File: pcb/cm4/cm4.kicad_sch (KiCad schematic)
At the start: 1 part, among them J101 Conn_02x10_Row_Letter_First

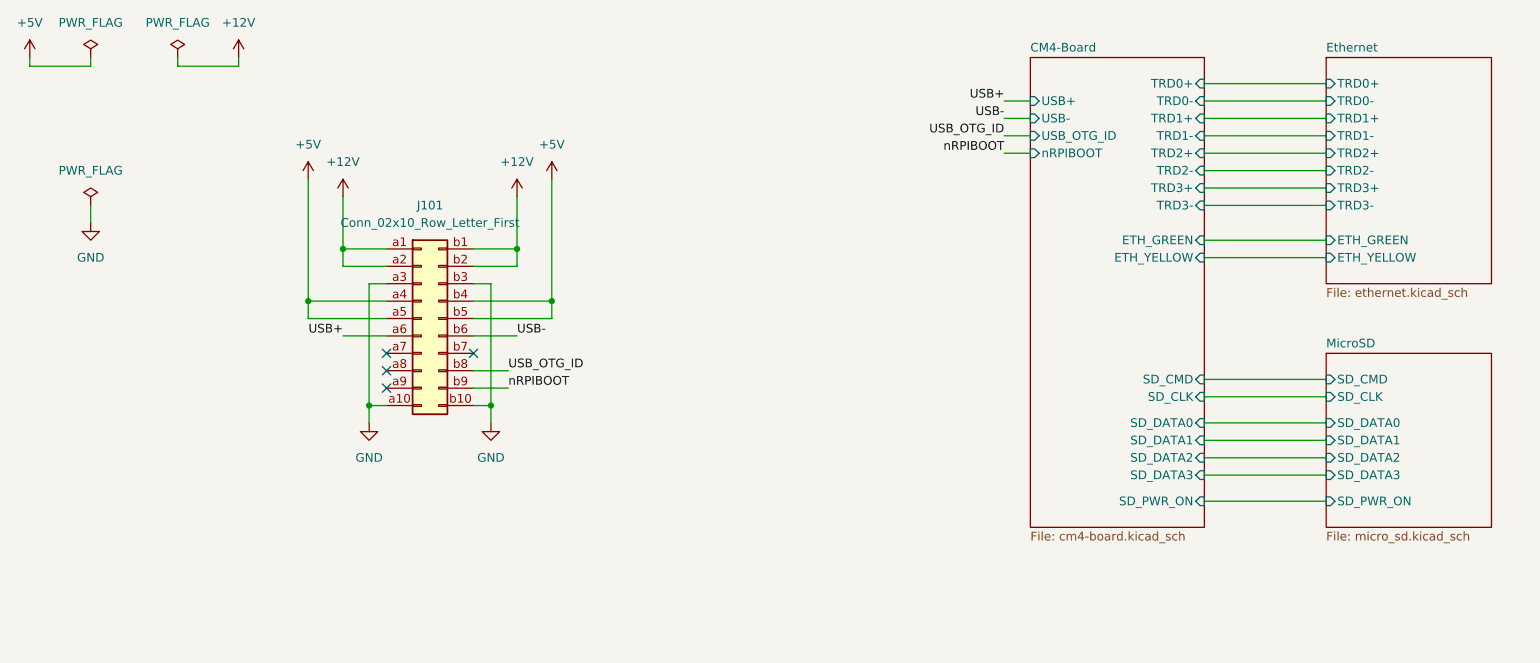
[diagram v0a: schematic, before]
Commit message: add i2c
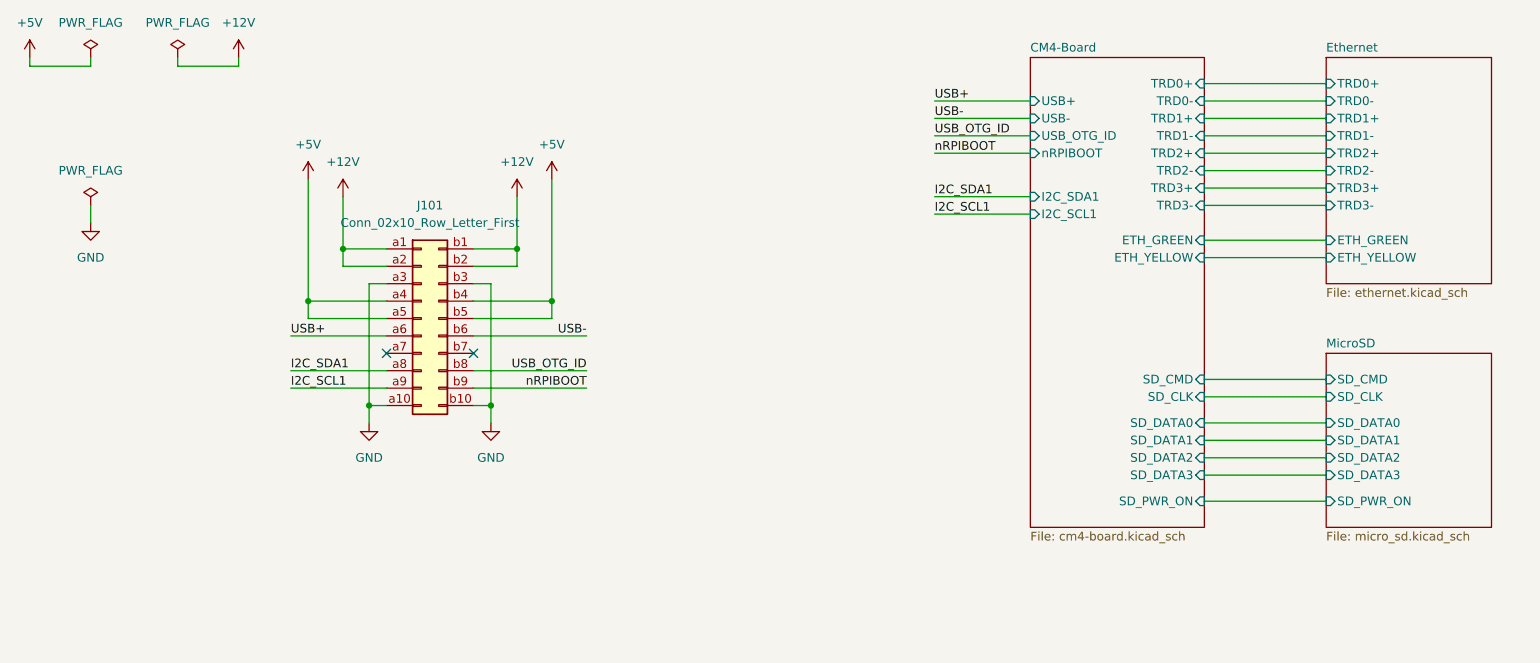
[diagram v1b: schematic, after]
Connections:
- net I2C_SDA1: now reaches J101.a8 (Pin_a8)
- net I2C_SCL1: now reaches J101.a9 (Pin_a9)
- no-connect marks 4 -> 2
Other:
- sheet CM4-Board ports: added I2C_SCL1, I2C_SDA1; removed none
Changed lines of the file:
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@@
-	)
-	(no_connect
-		(at 76.2 115.57)
 	)
 	(no_connect
 		(at 76.2 113.03)
 	)
-	(no_connect
-		(at 76.2 118.11)
-	)
 	(wire
 		(pts
@@
 	(wire
 		(pts
-			(xy 166.37 78.74) (xy 170.18 78.74)
+			(xy 156.21 78.74) (xy 170.18 78.74)
 		)
 		(stroke
@@
 	(wire
 		(pts
-			(xy 69.85 110.49) (xy 76.2 110.49)
+			(xy 62.23 110.49) (xy 76.2 110.49)
 		)
 		(stroke
@@
 	(wire
 		(pts
-			(xy 166.37 83.82) (xy 170.18 83.82)
+			(xy 156.21 83.82) (xy 170.18 83.82)
 		)
 		(stroke
@@
 	(wire
 		(pts
-			(xy 166.37 76.2) (xy 170.18 76.2)
+			(xy 156.21 76.2) (xy 170.18 76.2)
 		)
 		(stroke
@@
 	(wire
 		(pts
-			(xy 88.9 118.11) (xy 93.98 118.11)
+			(xy 156.21 92.71) (xy 170.18 92.71)
+		)
+		(stroke
+			(width 0)
+			(type default)
+		)
+	)
+	(wire
+		(pts
+			(xy 156.21 90.17) (xy 170.18 90.17)
+		)
+		(stroke
+			(width 0)
+			(type default)
+		)
+	)
+	(wire
+		(pts
+			(xy 88.9 118.11) (xy 105.41 118.11)
 		)
 		(stroke
@@
 	(wire
 		(pts
+			(xy 62.23 118.11) (xy 76.2 118.11)
+		)
+		(stroke
+			(width 0)
+			(type default)
+		)
+	)
+	(wire
+		(pts
 			(xy 95.25 97.79) (xy 95.25 90.17)
 		)
@@
 	(wire
 		(pts
+			(xy 62.23 115.57) (xy 76.2 115.57)
+		)
+		(stroke
+			(width 0)
+			(type default)
+		)
+	)
+	(wire
+		(pts
 			(xy 95.25 100.33) (xy 95.25 97.79)
 		)
@@
 	(wire
 		(pts
-			(xy 166.37 81.28) (xy 170.18 81.28)
+			(xy 156.21 81.28) (xy 170.18 81.28)
 		)
 		(stroke
@@
 	(wire
 		(pts
-			(xy 88.9 115.57) (xy 93.98 115.57)
+			(xy 88.9 115.57) (xy 105.41 115.57)
 		)
 		(stroke
@@
 	(wire
 		(pts
-			(xy 88.9 110.49) (xy 95.25 110.49)
-		)
-		(stroke
-			(width 0)
-			(type default)
-		)
-	)
-	(label "USB_OTG_ID"
-		(at 93.98 115.57 0)
+			(xy 88.9 110.49) (xy 105.41 110.49)
+		)
+		(stroke
+			(width 0)
+			(type default)
+		)
+	)
+	(label "I2C_SDA1"
+		(at 156.21 90.17 0)
 		(effects
 			(font
@@
 		)
 	)
-	(label "USB+"
-		(at 166.37 76.2 180)
+	(label "I2C_SCL1"
+		(at 156.21 92.71 0)
 		(effects
 			(font
 				(size 1.27 1.27)
 			)
-			(justify right bottom)
+			(justify left bottom)
 		)
 	)
 	(label "USB_OTG_ID"
-		(at 166.37 81.28 180)
+		(at 105.41 115.57 180)
 		(effects
 			(font
@@
 	)
 	(label "USB+"
-		(at 69.85 110.49 180)
+		(at 156.21 76.2 0)
 		(effects
 			(font
 				(size 1.27 1.27)
 			)
-			(justify right bottom)
-		)
-	)
-	(label "USB-"
-		(at 166.37 78.74 180)
+			(justify left bottom)
+		)
+	)
+	(label "I2C_SDA1"
+		(at 62.23 115.57 0)
 		(effects
 			(font
 				(size 1.27 1.27)
 			)
-			(justify right bottom)
-		)
-	)
-	(label "nRPIBOOT"
-		(at 166.37 83.82 180)
+			(justify left bottom)
+		)
+	)
+	(label "USB_OTG_ID"
+		(at 156.21 81.28 0)
 		(effects
 			(font
 				(size 1.27 1.27)
 			)
-			(justify right bottom)
-		)
-	)
-	(label "USB-"
-		(at 95.25 110.49 0)
+			(justify left bottom)
+		)
+	)
+	(label "USB+"
+		(at 62.23 110.49 0)
 		(effects
 			(font
@@
 		)
 	)
+	(label "USB-"
+		(at 156.21 78.74 0)
+		(effects
+			(font
+				(size 1.27 1.27)
+			)
+			(justify left bottom)
+		)
+	)
 	(label "nRPIBOOT"
-		(at 93.98 118.11 0)
+		(at 156.21 83.82 0)
+		(effects
+			(font
+				(size 1.27 1.27)
+			)
+			(justify left bottom)
+		)
+	)
+	(label "USB-"
+		(at 105.41 110.49 180)
+		(effects
+			(font
+				(size 1.27 1.27)
+			)
+			(justify right bottom)
+		)
+	)
+	(label "nRPIBOOT"
+		(at 105.41 118.11 180)
+		(effects
+			(font
+				(size 1.27 1.27)
+			)
+			(justify right bottom)
+		)
+	)
+	(label "I2C_SCL1"
+		(at 62.23 118.11 0)
 		(effects
 			(font
@@
 			)
 		)
+		(pin "I2C_SDA1" input
+			(at 170.18 90.17 180)
+			(effects
+				(font
+					(size 1.27 1.27)
+				)
+				(justify left)
+			)
+		)
+		(pin "I2C_SCL1" input
+			(at 170.18 92.71 180)
+			(effects
+				(font
+					(size 1.27 1.27)
+				)
+				(justify left)
+			)
+		)

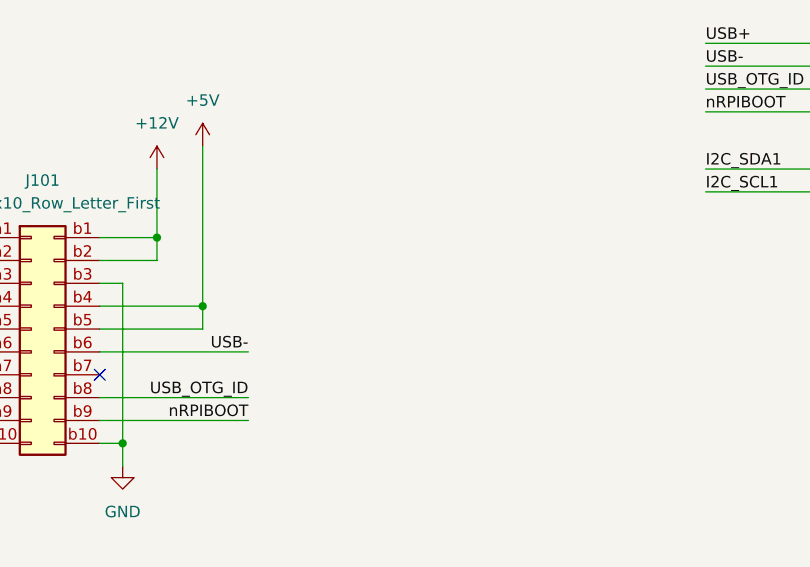
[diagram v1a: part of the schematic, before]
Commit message: add more caps
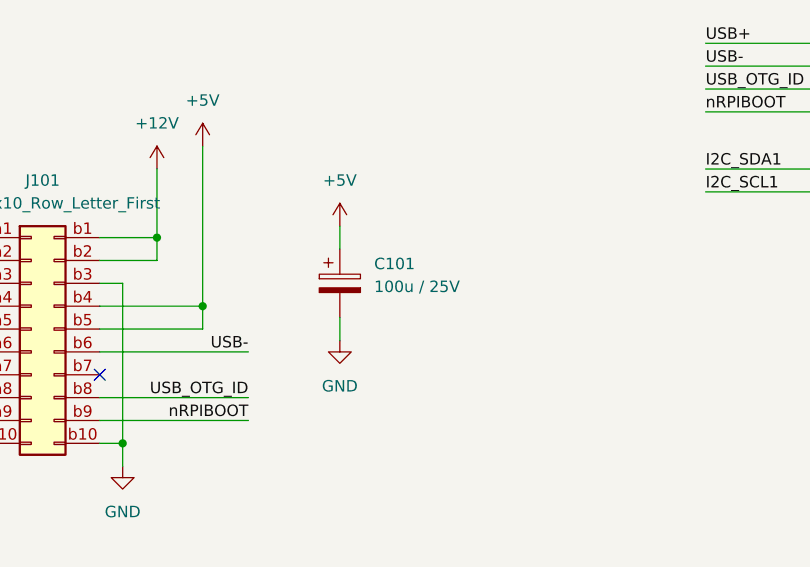
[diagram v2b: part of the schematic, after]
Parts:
- added C101: 100u / 25V, Capacitor_Tantalum_SMD:CP_EIA-7343-43_Kemet-X_Pad2.25x2.55mm_HandSolder, symbol Device:C_Polarized
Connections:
- net +5V: now also C101.1
- net GND: now also C101.2
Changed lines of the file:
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@@
+	(wire
+		(pts
+			(xy 115.57 106.68) (xy 115.57 109.22)
+		)
+		(stroke
+			(width 0)
+			(type default)
+		)
+	)
 	(wire
 		(pts
@@
 		(pts
 			(xy 195.58 125.73) (xy 213.36 125.73)
+		)
+		(stroke
+			(width 0)
+			(type default)
+		)
+	)
+	(wire
+		(pts
+			(xy 115.57 96.52) (xy 115.57 99.06)
 		)
 		(stroke
@@
 	)
 	(symbol
+		(lib_id "Device:C_Polarized")
+		(at 115.57 102.87 0)
+		(unit 1)
+		(exclude_from_sim no)
+		(in_bom yes)
+		(on_board yes)
+		(dnp no)
+		(fields_autoplaced yes)
+		(property "Reference" "C101"
+			(at 119.38 100.7109 0)
+			(effects
+				(font
+					(size 1.27 1.27)
+				)
+				(justify left)
+			)
+		)
+		(property "Value" "100u / 25V"
+			(at 119.38 103.2509 0)
+			(effects
+				(font
+					(size 1.27 1.27)
+				)
+				(justify left)
+			)
+		)
+		(property "Footprint" "Capacitor_Tantalum_SMD:CP_EIA-7343-43_Kemet-X_Pad2.25x2.55mm_HandSolder"
+			(at 116.5352 106.68 0)
+			(effects
+				(font
+					(size 1.27 1.27)
+				)
+				(hide yes)
+			)
+		)
+		(property "Datasheet" "~"
+			(at 115.57 102.87 0)
+			(effects
+				(font
+					(size 1.27 1.27)
+				)
+				(hide yes)
+			)
+		)
+		(property "Description" "Polarized capacitor"
+			(at 115.57 102.87 0)
+			(effects
+				(font
+					(size 1.27 1.27)
+				)
+				(hide yes)
+			)
+		)
+		(property "LCSC" "C7230"
+			(at 115.57 102.87 0)
+			(effects
+				(font
+					(size 1.27 1.27)
+				)
+				(hide yes)
+			)
+		)
+		(pin "2"
+		)
+		(pin "1"
+		)
+		(instances
+			(project "cm4"
+				(path "/5d20b266-567e-45c6-9e3e-145c2aea1daa"
+					(reference "C101")
+					(unit 1)
+				)
+			)
+		)
+	)
+	(symbol
 		(lib_id "power:GND")
 		(at 91.44 123.19 0)
@@
 	)
 	(symbol
+		(lib_id "power:GND")
+		(at 115.57 109.22 0)
+		(unit 1)
+		(exclude_from_sim no)
+		(in_bom yes)
+		(on_board yes)
+		(dnp no)
+		(fields_autoplaced yes)
+		(property "Reference" "#PWR0111"
+			(at 115.57 115.57 0)
+			(effects
+				(font
+					(size 1.27 1.27)
+				)
+				(hide yes)
+			)
+		)
+		(property "Value" "GND"
+			(at 115.57 114.3 0)
+			(effects
+				(font
+					(size 1.27 1.27)
+				)
+			)
+		)
+		(property "Footprint" ""
+			(at 115.57 109.22 0)
+			(effects
+				(font
+					(size 1.27 1.27)
+				)
+				(hide yes)
+			)
+		)
+		(property "Datasheet" ""
+			(at 115.57 109.22 0)
+			(effects
+				(font
+					(size 1.27 1.27)
+				)
+				(hide yes)
+			)
+		)
+		(property "Description" "Power symbol creates a global label with name \"GND\" , ground"
+			(at 115.57 109.22 0)
+			(effects
+				(font
+					(size 1.27 1.27)
+				)
+				(hide yes)
+			)
+		)
+		(pin "1"
+		)
+		(instances
+			(project "cm4"
+				(path "/5d20b266-567e-45c6-9e3e-145c2aea1daa"
+					(reference "#PWR0111")
+					(unit 1)
+				)
+			)
+		)
+	)
+	(symbol
 		(lib_id "power:+5V")
 		(at 64.77 87.63 0)
@@
 					(unit 1)
 				)
+			)
+		)
+	)
+	(symbol
+		(lib_id "power:+5V")
+		(at 115.57 96.52 0)
+		(unit 1)
+		(exclude_from_sim no)
+		(in_bom yes)
+		(on_board yes)
+		(dnp no)
+		(fields_autoplaced yes)
+		(property "Reference" "#PWR0110"
+			(at 115.57 100.33 0)
+			(effects
+				(font
+					(size 1.27 1.27)
+				)
+				(hide yes)
+			)
+		)
+		(property "Value" "+5V"
+			(at 115.57 91.44 0)
+			(effects
+				(font
+					(size 1.27 1.27)
+				)
+			)
+		)
+		(property "Footprint" ""
+			(at 115.57 96.52 0)
+			(effects
+				(font
+					(size 1.27 1.27)
+				)
+				(hide yes)
+			)
+		)
+		(property "Datasheet" ""
+			(at 115.57 96.52 0)
+			(effects
+				(font
+					(size 1.27 1.27)
+				)
+				(hide yes)
+			)
+		)
+		(property "Description" "Power symbol creates a global label with name \"+5V\""
+			(at 115.57 96.52 0)
+			(effects
+				(font
+					(size 1.27 1.27)
+				)
+				(hide yes)
+			)
+		)
+		(property "LCSC" ""
+			(at 115.57 96.52 0)
+			(effects
+				(font
+					(size 1.27 1.27)
+				)
+				(hide yes)
+			)
+		)
+		(pin "1"
+		)
+		(instances
+			(project "cm4"
+				(path "/5d20b266-567e-45c6-9e3e-145c2aea1daa"
+					(reference "#PWR0110")
+					(unit 1)
+				)

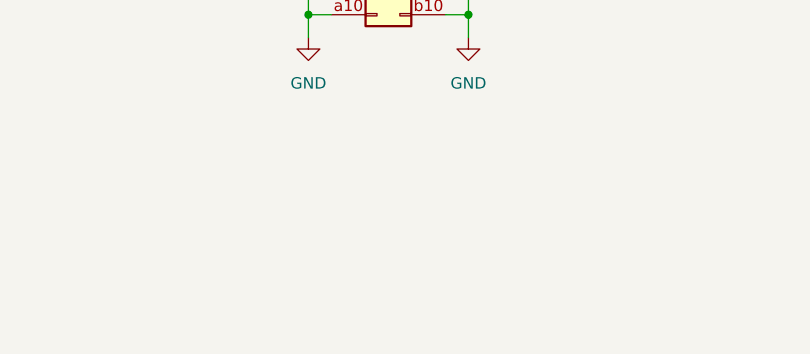
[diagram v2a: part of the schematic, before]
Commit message: update pcb size
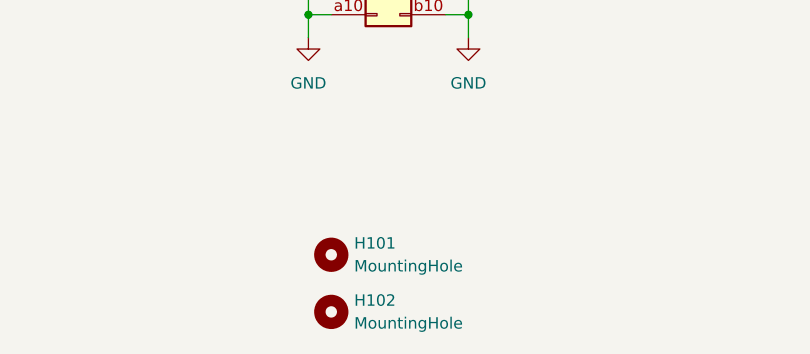
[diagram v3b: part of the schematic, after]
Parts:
- added H101, H102: MountingHole, MountingHole:MountingHole_2.7mm_M2.5, symbol Mechanical:MountingHole
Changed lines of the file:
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@@
+	)
+	(symbol
+		(lib_id "Mechanical:MountingHole")
+		(at 76.2 147.32 0)
+		(unit 1)
+		(exclude_from_sim yes)
+		(in_bom no)
+		(on_board yes)
+		(dnp no)
+		(fields_autoplaced yes)
+		(property "Reference" "H101"
+			(at 78.74 146.0499 0)
+			(effects
+				(font
+					(size 1.27 1.27)
+				)
+				(justify left)
+			)
+		)
+		(property "Value" "MountingHole"
+			(at 78.74 148.5899 0)
+			(effects
+				(font
+					(size 1.27 1.27)
+				)
+				(justify left)
+			)
+		)
+		(property "Footprint" "MountingHole:MountingHole_2.7mm_M2.5"
+			(at 76.2 147.32 0)
+			(effects
+				(font
+					(size 1.27 1.27)
+				)
+				(hide yes)
+			)
+		)
+		(property "Datasheet" "~"
+			(at 76.2 147.32 0)
+			(effects
+				(font
+					(size 1.27 1.27)
+				)
+				(hide yes)
+			)
+		)
+		(property "Description" "Mounting Hole without connection"
+			(at 76.2 147.32 0)
+			(effects
+				(font
+					(size 1.27 1.27)
+				)
+				(hide yes)
+			)
+		)
+		(property "LCSC" ""
+			(at 76.2 147.32 0)
+			(effects
+				(font
+					(size 1.27 1.27)
+				)
+				(hide yes)
+			)
+		)
+		(instances
+			(project "cm4"
+				(path "/5d20b266-567e-45c6-9e3e-145c2aea1daa"
+					(reference "H101")
+					(unit 1)
+				)
+			)
+		)
 	)
 	(symbol
@@
 					(unit 1)
 				)
+			)
+		)
+	)
+	(symbol
+		(lib_id "Mechanical:MountingHole")
+		(at 76.2 153.67 0)
+		(unit 1)
+		(exclude_from_sim yes)
+		(in_bom no)
+		(on_board yes)
+		(dnp no)
+		(fields_autoplaced yes)
+		(property "Reference" "H102"
+			(at 78.74 152.3999 0)
+			(effects
+				(font
+					(size 1.27 1.27)
+				)
+				(justify left)
+			)
+		)
+		(property "Value" "MountingHole"
+			(at 78.74 154.9399 0)
+			(effects
+				(font
+					(size 1.27 1.27)
+				)
+				(justify left)
+			)
+		)
+		(property "Footprint" "MountingHole:MountingHole_2.7mm_M2.5"
+			(at 76.2 153.67 0)
+			(effects
+				(font
+					(size 1.27 1.27)
+				)
+				(hide yes)
+			)
+		)
+		(property "Datasheet" "~"
+			(at 76.2 153.67 0)
+			(effects
+				(font
+					(size 1.27 1.27)
+				)
+				(hide yes)
+			)
+		)
+		(property "Description" "Mounting Hole without connection"
+			(at 76.2 153.67 0)
+			(effects
+				(font
+					(size 1.27 1.27)
+				)
+				(hide yes)
+			)
+		)
+		(property "LCSC" ""
+			(at 76.2 153.67 0)
+			(effects
+				(font
+					(size 1.27 1.27)
+				)
+				(hide yes)
+			)
+		)
+		(instances
+			(project ""
+				(path "/5d20b266-567e-45c6-9e3e-145c2aea1daa"
+					(reference "H102")
+					(unit 1)
+				)

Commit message: fixes
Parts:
- H101, H102: footprint MountingHole:MountingHole_2.7mm_M2.5 -> MountingHole:MountingHole_3.2mm_M3
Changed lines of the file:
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@@
 			)
 		)
-		(property "Footprint" "MountingHole:MountingHole_2.7mm_M2.5"
+		(property "Footprint" "MountingHole:MountingHole_3.2mm_M3"
 			(at 76.2 147.32 0)
 			(effects
@@
 			)
 		)
-		(property "Footprint" "MountingHole:MountingHole_2.7mm_M2.5"
+		(property "Footprint" "MountingHole:MountingHole_3.2mm_M3"
 			(at 76.2 153.67 0)
 			(effects

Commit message: update cm4 board
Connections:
- net USB+ renamed USB_DP
- net USB- renamed USB_DM
- net USB_OTG_ID renamed USB_ID
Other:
- sheet CM4-Board ports: added ETH_LED_G, ETH_LED_Y, ETH_TRD0_M, ETH_TRD0_P, ETH_TRD1_M, ETH_TRD1_P, ETH_TRD2_M, ETH_TRD2_P, ETH_TRD3_M, ETH_TRD3_P, USB_DM, USB_DP, USB_ID; removed ETH_GREEN, ETH_YELLOW, TRD0+, TRD0-, TRD1+, TRD1-, TRD2+, TRD2-, TRD3+, TRD3-, USB+, USB-, USB_OTG_ID
- sheet Ethernet ports: added ETH_LED_G, ETH_LED_Y, ETH_TRD0_M, ETH_TRD0_P, ETH_TRD1_M, ETH_TRD1_P, ETH_TRD2_M, ETH_TRD2_P, ETH_TRD3_M, ETH_TRD3_P; removed ETH_GREEN, ETH_YELLOW, TRD0+, TRD0-, TRD1+, TRD1-, TRD2+, TRD2-, TRD3+, TRD3-

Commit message: update ALL parts
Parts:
- C101: footprint Capacitor_Tantalum_SMD:CP_EIA-7343-43_Kemet-X_Pad2.25x2.55mm_HandSolder -> Capacitor_Tantalum_SMD:CP_EIA-7343-43_Kemet-X; LCSC C7230 -> C132558
- J101: MOUSER (none) -> 798-PCN10C20S254DS72
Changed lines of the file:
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@@
 			)
 		)
-		(property "Footprint" "Capacitor_Tantalum_SMD:CP_EIA-7343-43_Kemet-X_Pad2.25x2.55mm_HandSolder"
+		(property "Footprint" "Capacitor_Tantalum_SMD:CP_EIA-7343-43_Kemet-X"
 			(at 116.5352 106.68 0)
 			(effects
@@
 			)
 		)
-		(property "LCSC" "C7230"
+		(property "LCSC" "C132558"
 			(at 115.57 102.87 0)
 			(effects
@@
 				)
 				(hide yes)
+			)
+		)
+		(property "MOUSER" ""
+			(at 115.57 102.87 0)
+			(effects
+				(font
+					(size 1.27 1.27)
+				)
 			)
 		)
@@
 			)
 		)
+		(property "MOUSER" ""
+			(at 76.2 147.32 0)
+			(effects
+				(font
+					(size 1.27 1.27)
+				)
+			)
+		)
 		(instances
 			(project "cm4"
@@
 			)
 		)
+		(property "MOUSER" "798-PCN10C20S254DS72"
+			(at 81.28 107.95 0)
+			(effects
+				(font
+					(size 1.27 1.27)
+				)
+			)
+		)
 		(pin "a5"
 		)
@@
 			)
 		)
+		(property "MOUSER" ""
+			(at 76.2 153.67 0)
+			(effects
+				(font
+					(size 1.27 1.27)
+				)
+			)
+		)
